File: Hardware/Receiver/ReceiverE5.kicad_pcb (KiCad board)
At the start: 2 copper layers, 37 parts, among them J1 KBUS, J2 AVR-PDI-6A, J3 CONN_01X08, J4 CONN_01X06, J5 CONN_01X06, J6 CONN_01X04, J7 CONN_01X04, U1 ATXMEGA32E5-A, U2 LM2731, U3 SN74LV07A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

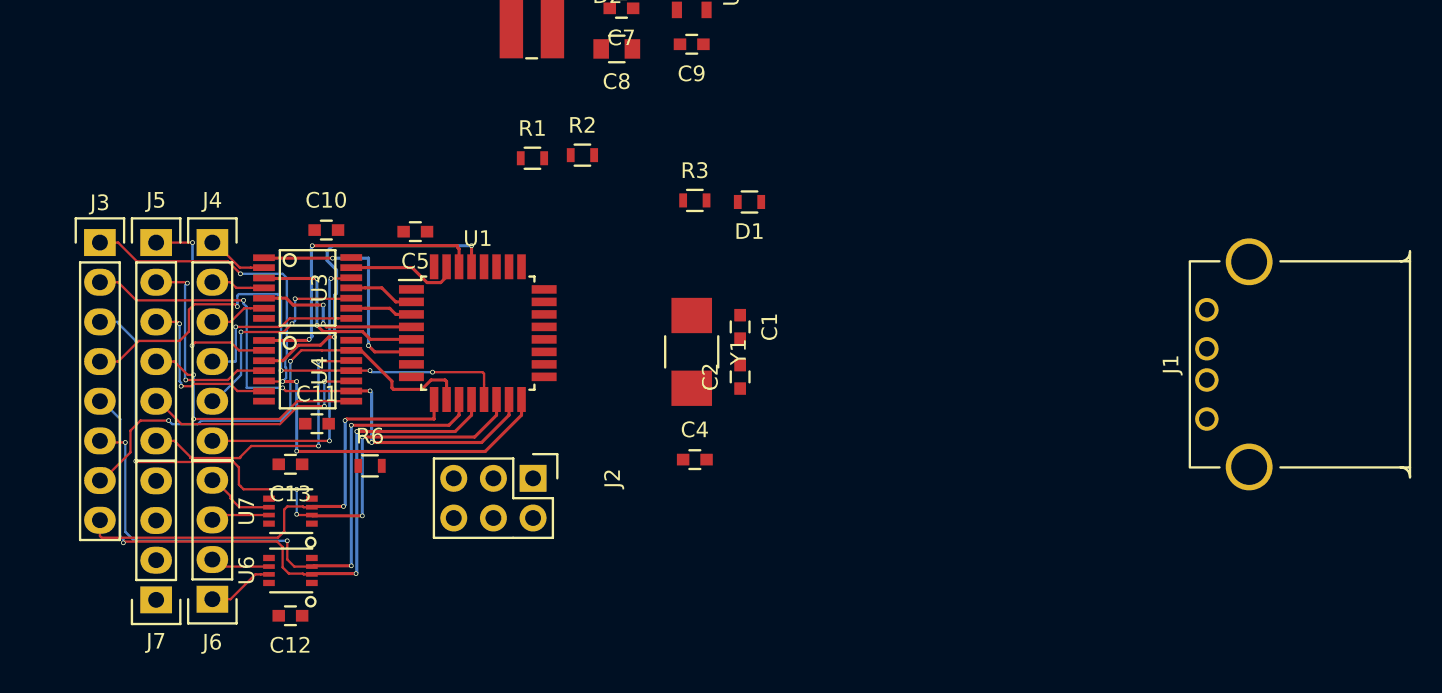
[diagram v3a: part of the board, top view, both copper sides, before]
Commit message: Added mounting holes
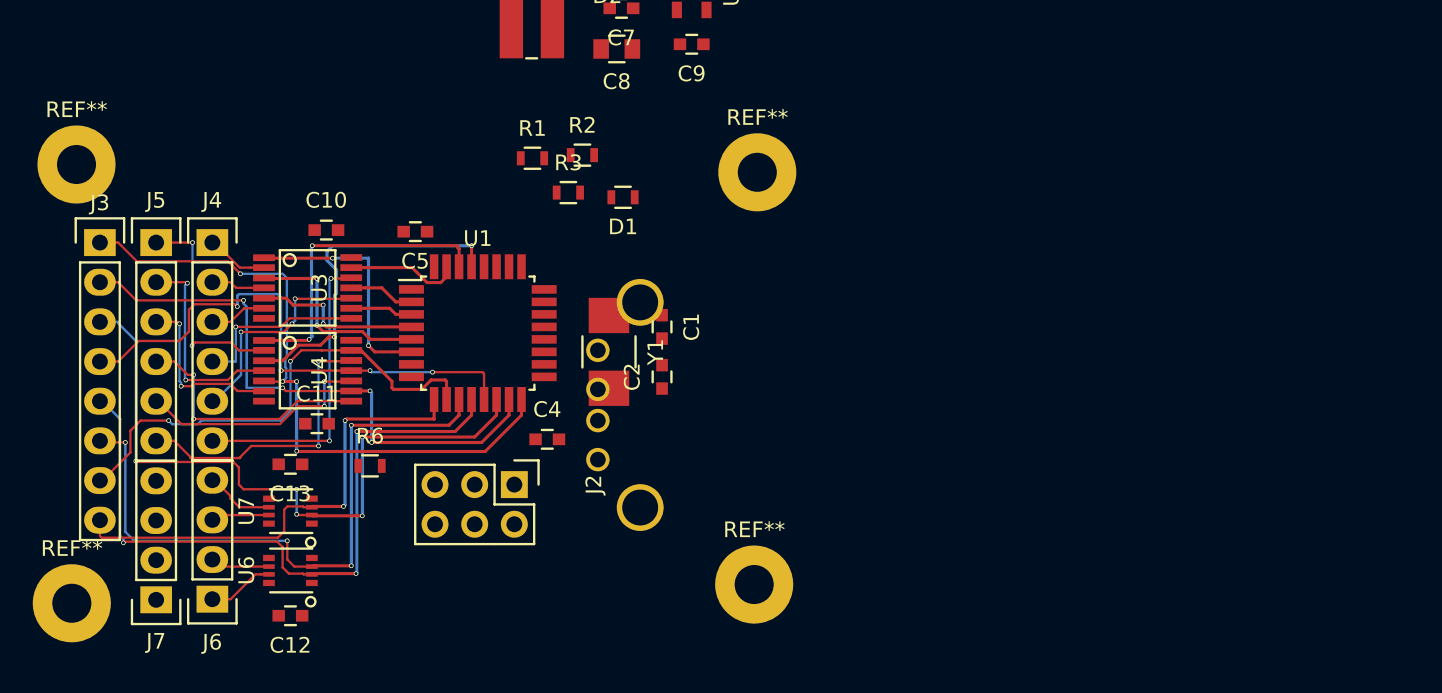
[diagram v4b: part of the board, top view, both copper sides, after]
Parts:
- added REF**: MountingHole_2.5mm_Pad, Mounting_Holes:MountingHole_2.5mm_Pad, F.Cu at (114.2, 61.5)
- added REF**: MountingHole_2.5mm_Pad, Mounting_Holes:MountingHole_2.5mm_Pad, F.Cu at (114.0, 87.9)
- added REF**: MountingHole_2.5mm_Pad, Mounting_Holes:MountingHole_2.5mm_Pad, F.Cu at (70.3, 89.1)
- added REF**: MountingHole_2.5mm_Pad, Mounting_Holes:MountingHole_2.5mm_Pad, F.Cu at (70.6, 61.0)
- J1: moved to B.Cu
- moved J1 39.1 mm to (106.7, 76.4), turned to 270 degrees
- moved C4 9.54 mm to (100.8, 78.6)
- moved R3 8.12 mm to (102.1, 62.8)
- moved D1 8.11 mm to (105.6, 63.1)
- moved Y1 5.30 mm to (104.7, 73.0)
- moved C1 5.00 mm to (108.1, 71.4)
- moved C2 5.00 mm to (108.1, 74.6)
- moved J2 1.26 mm to (98.6, 81.5)
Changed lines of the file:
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@@
 (kicad_pcb (version 4) (host pcbnew 4.0.2-stable)
   (general
-    (links 119)
+    (links 0)
     (no_connects 119)
     (area 0 0 0 0)
     (thickness 1.6)
-    (drawings 0)
+    (drawings 1)
     (tracks 369)
     (zones 0)
-    (modules 37)
+    (modules 41)
     (nets 51)
   )
@@
     (add_net "Net-(R3-Pad1)")
   )
+  (module Mounting_Holes:MountingHole_2.5mm_Pad (layer F.Cu)
+    (at 114.2 61.5)
+    (descr "Mounting Hole 2.5mm")
+    (tags "mounting hole 2.5mm")
+    (fp_text reference REF** (at 0 -3.5) (layer F.SilkS)
+      (effects (font (size 1 1) (thickness 0.15)))
+    )
+    (fp_text value MountingHole_2.5mm_Pad (at 0 3.5) (layer F.Fab)
+      (effects (font (size 1 1) (thickness 0.15)))
+    )
+    (fp_circle (center 0 0) (end 2.5 0) (layer Cmts.User) (width 0.15))
+    (fp_circle (center 0 0) (end 2.75 0) (layer F.CrtYd) (width 0.05))
+    (pad 1 thru_hole circle (at 0 0) (size 5 5) (drill 2.5) (layers *.Cu *.Mask))
+  )
+  (module Mounting_Holes:MountingHole_2.5mm_Pad (layer F.Cu)
+    (at 114 87.9)
+    (descr "Mounting Hole 2.5mm")
+    (tags "mounting hole 2.5mm")
+    (fp_text reference REF** (at 0 -3.5) (layer F.SilkS)
+      (effects (font (size 1 1) (thickness 0.15)))
+    )
+    (fp_text value MountingHole_2.5mm_Pad (at 0 3.5) (layer F.Fab)
+      (effects (font (size 1 1) (thickness 0.15)))
+    )
+    (fp_circle (center 0 0) (end 2.5 0) (layer Cmts.User) (width 0.15))
+    (fp_circle (center 0 0) (end 2.75 0) (layer F.CrtYd) (width 0.05))
+    (pad 1 thru_hole circle (at 0 0) (size 5 5) (drill 2.5) (layers *.Cu *.Mask))
+  )
+  (module Mounting_Holes:MountingHole_2.5mm_Pad (layer F.Cu)
+    (at 70.3 89.1)
+    (descr "Mounting Hole 2.5mm")
+    (tags "mounting hole 2.5mm")
+    (fp_text reference REF** (at 0 -3.5) (layer F.SilkS)
+      (effects (font (size 1 1) (thickness 0.15)))
+    )
+    (fp_text value MountingHole_2.5mm_Pad (at 0 3.5) (layer F.Fab)
+      (effects (font (size 1 1) (thickness 0.15)))
+    )
+    (fp_circle (center 0 0) (end 2.5 0) (layer Cmts.User) (width 0.15))
+    (fp_circle (center 0 0) (end 2.75 0) (layer F.CrtYd) (width 0.05))
+    (pad 1 thru_hole circle (at 0 0) (size 5 5) (drill 2.5) (layers *.Cu *.Mask))
+  )
   (module kuro:VSSOP8_SOT765-1 (layer F.Cu)
     (at 84.3 83.2 90)
@@
   )
   (module Capacitors_SMD:C_0603 (layer F.Cu)
-    (at 113.1 71.4 270)
+    (at 108.1 71.4 270)
     (descr "Capacitor SMD 0603, reflow soldering, AVX (see smccp.pdf)")
     (tags "capacitor 0603")
@@
   )
   (module Capacitors_SMD:C_0603 (layer F.Cu)
-    (at 113.1 74.6 90)
+    (at 108.1 74.6 90)
     (descr "Capacitor SMD 0603, reflow soldering, AVX (see smccp.pdf)")
     (tags "capacitor 0603")
@@
   )
   (module Capacitors_SMD:C_0603 (layer F.Cu)
-    (at 110.2 79.9)
+    (at 100.75 78.6)
     (descr "Capacitor SMD 0603, reflow soldering, AVX (see smccp.pdf)")
     (tags "capacitor 0603")
@@
   )
   (module Resistors_SMD:R_0603 (layer F.Cu)
-    (at 113.7 63.4 180)
+    (at 105.6 63.1 180)
     (descr "Resistor SMD 0603, reflow soldering, Vishay (see dcrcw.pdf)")
     (tags "resistor 0603")
@@
     )
   )
-  (module kuro:USB_A_multicomp (layer F.Cu)
-    (at 145.7 73.8 90)
+  (module kuro:USB_A_multicomp (layer B.Cu)
+    (at 106.7 76.4 270)
     (descr "FCI 87520")
     (tags "USB USB_A")
-    (fp_text reference J1 (at 0 -5 90) (layer F.SilkS)
-      (effects (font (size 1 1) (thickness 0.15)))
-    )
-    (fp_text value KBUS (at 0.33794 4.73458 90) (layer F.Fab)
-      (effects (font (size 1 1) (thickness 0.15)))
-    )
-    (fp_arc (start 7.2 9.7) (end 7.2 10.3) (angle 90) (layer F.SilkS) (width 0.15))
-    (fp_line (start -7.25 10.3) (end 7.25 10.3) (layer F.SilkS) (width 0.15))
-    (fp_line (start -6.6 2) (end -6.6 10.3) (layer F.SilkS) (width 0.15))
-    (fp_line (start 6.6 -3.8) (end 6.6 -1.9) (layer F.SilkS) (width 0.15))
-    (fp_line (start -6.6 -3.8) (end -6.6 -1.9) (layer F.SilkS) (width 0.15))
-    (fp_line (start -8.45 10.5) (end -8.45 -4.1) (layer F.CrtYd) (width 0.05))
-    (fp_line (start 8.45 -4.1) (end 8.45 10.5) (layer F.CrtYd) (width 0.05))
-    (fp_line (start -8.45 10.5) (end 8.45 10.5) (layer F.CrtYd) (width 0.05))
-    (fp_line (start -8.45 -4.1) (end 8.45 -4.1) (layer F.CrtYd) (width 0.05))
-    (fp_line (start 6.55 -3.8) (end -6.55 -3.8) (layer F.SilkS) (width 0.15))
-    (fp_line (start 6.6 2) (end 6.6 10.3) (layer F.SilkS) (width 0.15))
-    (fp_arc (start -7.2 9.7) (end -6.6 9.7) (angle 90) (layer F.SilkS) (width 0.15))
-    (pad 4 thru_hole circle (at 3.5 -2.71) (size 1.50114 1.50114) (drill 1) (layers *.Cu *.Mask)
-      (net 2 GND))
-    (pad 3 thru_hole circle (at 1 -2.71) (size 1.50114 1.50114) (drill 1) (layers *.Cu *.Mask)
+    (fp_text reference J1 (at 0 5 270) (layer B.SilkS)
+      (effects (font (size 1 1) (thickness 0.15)) (justify mirror))
+    )
+    (fp_text value KBUS (at 0.33794 -4.73458 270) (layer B.Fab)
+      (effects (font (size 1 1) (thickness 0.15)) (justify mirror))
+    )
+    (fp_arc (start 7.2 -9.7) (end 7.2 -10.3) (angle -90) (layer B.SilkS) (width 0.15))
+    (fp_line (start -7.25 -10.3) (end 7.25 -10.3) (layer B.SilkS) (width 0.15))
+    (fp_line (start -6.6 -2) (end -6.6 -10.3) (layer B.SilkS) (width 0.15))
+    (fp_line (start 6.6 3.8) (end 6.6 1.9) (layer B.SilkS) (width 0.15))
+    (fp_line (start -6.6 3.8) (end -6.6 1.9) (layer B.SilkS) (width 0.15))
+    (fp_line (start -8.45 -10.5) (end -8.45 4.1) (layer B.CrtYd) (width 0.05))
+    (fp_line (start 8.45 4.1) (end 8.45 -10.5) (layer B.CrtYd) (width 0.05))
+    (fp_line (start -8.45 -10.5) (end 8.45 -10.5) (layer B.CrtYd) (width 0.05))
+    (fp_line (start -8.45 4.1) (end 8.45 4.1) (layer B.CrtYd) (width 0.05))
+    (fp_line (start 6.55 3.8) (end -6.55 3.8) (layer B.SilkS) (width 0.15))
+    (fp_line (start 6.6 -2) (end 6.6 -10.3) (layer B.SilkS) (width 0.15))
+    (fp_arc (start -7.2 -9.7) (end -6.6 -9.7) (angle -90) (layer B.SilkS) (width 0.15))
+    (pad 4 thru_hole circle (at 3.5 2.71) (size 1.50114 1.50114) (drill 1) (layers *.Cu *.Mask)
+      (net 2 GND))
+    (pad 3 thru_hole circle (at 1 2.71) (size 1.50114 1.50114) (drill 1) (layers *.Cu *.Mask)
       (net 11 /KBUS_RX))
-    (pad 2 thru_hole circle (at -1 -2.71) (size 1.50114 1.50114) (drill 1) (layers *.Cu *.Mask)
+    (pad 2 thru_hole circle (at -1 2.71) (size 1.50114 1.50114) (drill 1) (layers *.Cu *.Mask)
       (net 12 /KBUS_TX))
-    (pad 1 thru_hole circle (at -3.5 -2.71) (size 1.50114 1.50114) (drill 1) (layers *.Cu *.Mask)
+    (pad 1 thru_hole circle (at -3.5 2.71) (size 1.50114 1.50114) (drill 1) (layers *.Cu *.Mask)
       (net 6 +5V))
     (pad 5 thru_hole circle (at 6.57 0) (size 2.99974 2.99974) (drill 2.3) (layers *.Cu *.Mask)
@@
   )
   (module Pin_Headers:Pin_Header_Straight_2x03 (layer F.Cu)
-    (at 99.84 81.1 270)
+    (at 98.64 81.5 270)
     (descr "Through hole pin header")
     (tags "pin header")
@@
   )
   (module Resistors_SMD:R_0603 (layer F.Cu)
-    (at 110.2 63.3)
+    (at 102.1 62.8)
     (descr "Resistor SMD 0603, reflow soldering, Vishay (see dcrcw.pdf)")
     (tags "resistor 0603")
@@
   )
   (module kuro:SMD_Crystal_Multi_QC6CB_7A_ABM7 (layer F.Cu)
-    (at 110 73 270)
+    (at 104.7 73 270)
     (descr "Multiple SMD crystal footprint.svg")
     (tags "QC6CB 7A ABM7")
@@
       (net 3 "Net-(C2-Pad1)"))
   )
+  (module Mounting_Holes:MountingHole_2.5mm_Pad (layer F.Cu)
+    (at 70.6 61)
+    (descr "Mounting Hole 2.5mm")
+    (tags "mounting hole 2.5mm")
+    (fp_text reference REF** (at 0 -3.5) (layer F.SilkS)
+      (effects (font (size 1 1) (thickness 0.15)))
+    )
+    (fp_text value MountingHole_2.5mm_Pad (at 0 3.5) (layer F.Fab)
+      (effects (font (size 1 1) (thickness 0.15)))
+    )
+    (fp_circle (center 0 0) (end 2.5 0) (layer Cmts.User) (width 0.15))
+    (fp_circle (center 0 0) (end 2.75 0) (layer F.CrtYd) (width 0.05))
+    (pad 1 thru_hole circle (at 0 0) (size 5 5) (drill 2.5) (layers *.Cu *.Mask))
+  )
+  (dimension 50 (width 0.3) (layer Eco1.User)
+    (gr_text "50.000 mm" (at 95.086733 49.844833) (layer Eco1.User)
+      (effects (font (size 1.5 1.5) (thickness 0.3)))
+    )
+    (feature1 (pts (xy 120.086733 49.844833) (xy 120.086733 49.844833)))
+    (feature2 (pts (xy 70.086733 49.844833) (xy 70.086733 49.844833)))
+    (crossbar (pts (xy 70.086733 49.844833) (xy 120.086733 49.844833)))
+    (arrow1a (pts (xy 120.086733 49.844833) (xy 118.960229 50.431254)))
+    (arrow1b (pts (xy 120.086733 49.844833) (xy 118.960229 49.258412)))
+    (arrow2a (pts (xy 70.086733 49.844833) (xy 71.213237 50.431254)))
+    (arrow2b (pts (xy 70.086733 49.844833) (xy 71.213237 49.258412)))
+  )
   (segment (start 84.7 74.9) (end 83.8 74.9) (width 0.2) (layer F.Cu) (net 15))
